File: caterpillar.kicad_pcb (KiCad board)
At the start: 2 copper layers, 20.2 x 20.2 mm, 32 parts, among them J1 Conn_ARM_JTAG_SWD_10, M1 Conn_01x02_Pin, M2 *, M3 Conn_01x02_Pin, U1 STBB1-APUR, U2 ASM330LHHTR, U3 DRV8212P, U4 ADP2503ACPZ-3.3-R7, U6 max5419leta+T

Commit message: rules: import design rules from Altium project ruleset
From altium_rules.RUL (36 rules, the importable subset):
- constraints: min track 4mil, min hole 4mil, hole-to-hole 9.75mil,
  copper-to-edge 10mil (was 0/disabled), min via dia 9mil
- solder mask expansion 4mil (was 0)
- new Power net class (12mil tracks) assigned to +3.3V/+BATT/VDC/GND
- caterpillar.kicad_dru: BLE_FEEDLINE scoped clearance (dormant until
  that class exists; its Altium width rule deliberately NOT imported -
  impedance-tuned to a different stackup) and 4mil courtyard clearance
- Default net class track width 0.2 -> 0.1524mm (6mil, user choice)
- remove stale radial dimension annotation on User.1
Altium autorouter rules (fanout/topology/priority) have no KiCad
equivalent; short-circuit/unrouted/antenna checks are built into DRC.
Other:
- rule pad_to_mask_clearance: 0 -> 0.1016
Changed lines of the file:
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@@
 			(dielectric_constraints no)
 		)
-		(pad_to_mask_clearance 0)
+		(pad_to_mask_clearance 0.1016)
 		(allow_soldermask_bridges_in_footprints no)
 		(tenting
@@
 		(capping no)
 		(filling no)
+		(zone_defaults)
 		(pcbplotparams
 			(layerselection 0x00000000_00000000_55555555_5555f550)
@@
 		)
 	)
-	(dimension
-		(type radial)
-		(layer "User.1")
-		(pts
-			(xy 118.2 100) (xy 128 99)
-		)
-		(leader_length 1.255801)
-		(format
-			(prefix "")
-			(suffix "")
-			(units 3)
-			(units_format 0)
-			(precision 6)
-			(suppress_zeroes yes)
-		)
-		(style
-			(thickness 0.1)
-			(arrow_length 0.5)
-			(text_position_mode 2)
-			(extension_offset 0.1)
-			(keep_text_aligned yes)
-		)
-		(gr_text "9.9"
-			(at 134.5 98.872519 0)
-			(layer "User.1")
-			(effects
-				(font
-					(size 1.5 1.5)
-					(thickness 0.3)
-				)
-			)
-		)
-	)

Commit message: reorganized design a lot for better space organization
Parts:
- removed 3.3V1, GND2, SCL1, SDA1: Conn_01x01_Pin, Connector_Wire:SolderWirePad_1x01_SMD_1x2mm
- removed M1: Conn_01x02_Pin, Connector_PinHeader_2.00mm:PinHeader_1x02_P2.00mm_Vertical
- removed M3: Conn_01x02_Pin, Connector_PinHeader_2.54mm:PinHeader_1x02_P2.54mm_Vertical
- added J2: SM02B-SRSS-TB_LF__SN_, SM02B-SRSS-TB:SM02BSRSSTBLFSN, F.Cu at (118.0, 107.8)
- added J3: Castellated_2PTH_P1.27mm, Castellated_2PTH_P1.27mm:Castellated_2PTH_P1.27mm, F.Cu at (111.3, 109.7)
- added J4: Castellated_2PTH_P1.27mm, Castellated_2PTH_P1.27mm:Castellated_2PTH_P1.27mm, F.Cu at (113.9, 109.7)
- C17, L1: moved to B.Cu
- moved U4 10.7 mm to (118.2, 107.7)
- moved L6 10.5 mm to (118.2, 104.5)
- moved C3 9.23 mm to (115.4, 105.5), turned to 90 degrees
- moved C11 8.83 mm to (113.8, 105.6), turned to 90 degrees
- moved U1 7.05 mm to (118.0, 97.7)
- moved C8 6.59 mm to (117.1, 102.2)
- moved L5 6.23 mm to (115.6, 92.4)
- moved U6 5.52 mm to (113.3, 98.5)
- moved L1 4.84 mm to (111.9, 91.8)
- moved C5 4.48 mm to (111.0, 102.3)
- moved C17 4.46 mm to (111.9, 94.7)
- moved C6 4.07 mm to (111.0, 105.5), turned to -90 degrees
- moved R4 3.87 mm to (112.4, 102.2), turned to 90 degrees
- moved C7 3.49 mm to (113.9, 102.2), turned to 90 degrees
- moved C1 3.19 mm to (117.2, 102.4)
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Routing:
- net GND: track 42.9 -> 6.13 mm, vias 10 -> 0
- net +3.3V: track 40.6 -> 5.80 mm, vias 6 -> 0
- net +BATT: track 20.6 -> 0.00 mm
- net /IMU_INT1: track 14.5 -> 0.00 mm, vias 2 -> 0
- net /SDA: track 10.3 -> 0.00 mm, vias 1 -> 0
- net /SCL: track 9.72 -> 0.00 mm, vias 1 -> 0
- net VDC: track 9.37 -> 0.00 mm, vias 1 -> 0
- net /IMU_INT2: track 8.47 -> 0.00 mm
- net /SHDN1: track 7.37 -> 0.00 mm, vias 1 -> 0
- net /OUT2: track 6.93 -> 0.00 mm
- net /OUT1: track 6.31 -> 0.00 mm
- net /FB: track 5.04 -> 0.00 mm
- net /IN2: track 1.61 -> 4.71 mm
- net /IN1: track 1.69 -> 4.24 mm
- net /M_SLP: track 1.77 -> 3.93 mm
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- added copper zone on In1.Cu, net GND
- removed copper zone on F.Cu, net +3.3V
- removed copper zone on F.Cu, net +BATT
- removed copper zone on B.Cu, net GND
- removed copper zone on F.Cu, net VDC
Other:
- board size 20.2 x 20.2 mm -> 18.3 x 20.3 mm
- copper layers 2 -> 4

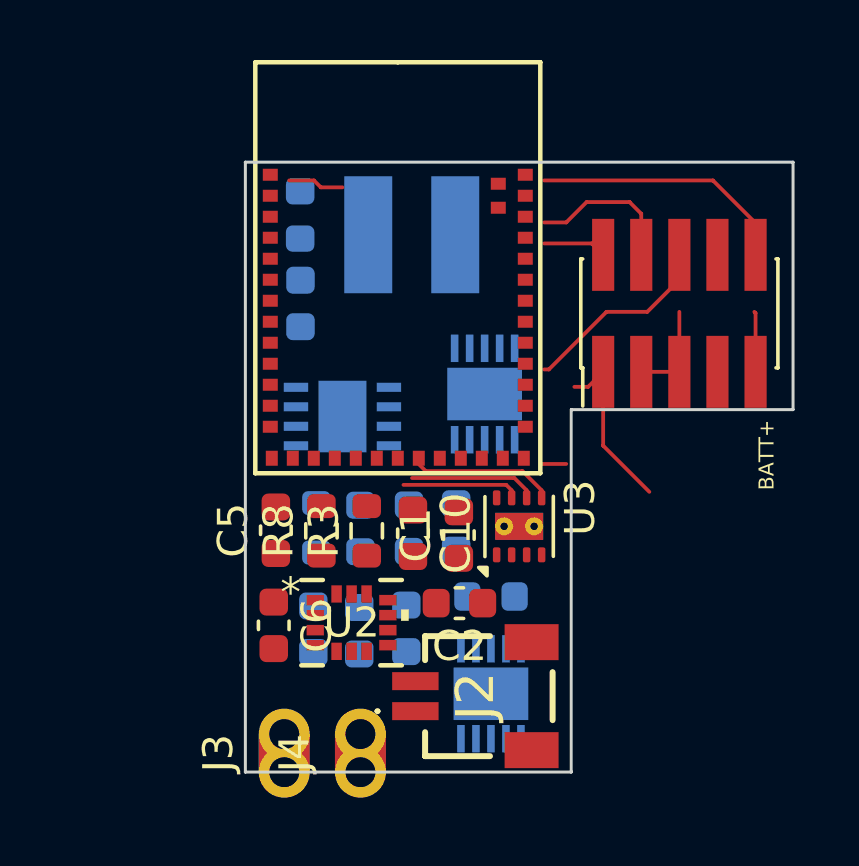
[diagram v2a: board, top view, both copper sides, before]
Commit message: component position&orientation adjusted further.
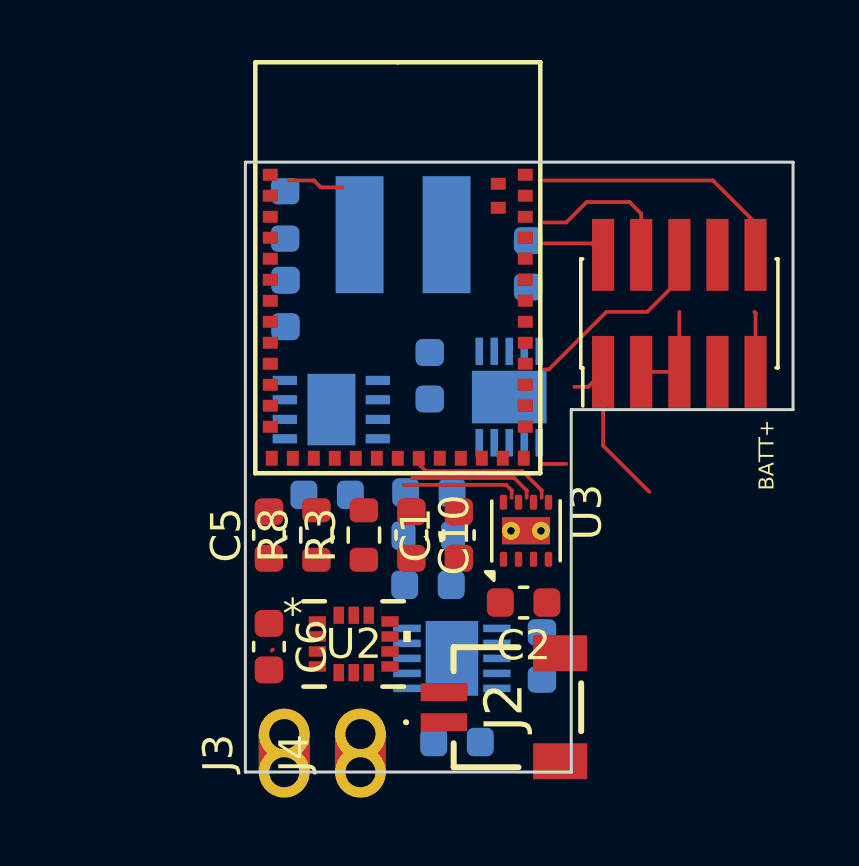
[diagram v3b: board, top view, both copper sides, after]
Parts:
- moved C11 13.5 mm to (119.5, 93.4)
- moved C9 5.13 mm to (116.2, 97.1), turned to -90 degrees
- moved C12 4.50 mm to (112.8, 101.1), turned to 180 degrees
- moved C3 4.15 mm to (117.1, 109.3), turned to 0 degrees
- moved R4 3.74 mm to (116.1, 102.5), turned to 0 degrees
- moved L6 2.61 mm to (119.9, 106.5), turned to 90 degrees
- moved C7 2.58 mm to (116.2, 101.0), turned to 0 degrees
- moved C8 2.15 mm to (116.1, 104.1), turned to 180 degrees
- moved C2 2.14 mm to (119.3, 104.7)
- moved U4 1.76 mm to (116.9, 106.5), turned to 180 degrees
- moved J2 1.02 mm to (118.9, 108.2)
- moved U1 0.83 mm to (118.8, 97.8)
- moved C6 0.73 mm to (110.8, 106.2)
- moved U2 0.71 mm to (113.6, 106.1)
- moved C17 0.50 mm to (111.4, 94.7)
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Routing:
- net /IN1: track 4.24 -> 0.00 mm
- net +3.3V: track 5.80 -> 9.74 mm

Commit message: pcb: sync with rev-2 schematic; bom: regenerate with MPN fields
- Board updated from schematic (re-linked by reference): C3/C6 uuid
  links repaired, orphan C7 footprint removed, R7/R9/C13/R5/R6 placed
  onto the board (placement/routing to follow)
- BOM regenerated from the current schematic (old caterpillar.csv was
  a stale Muscle_PCB-era export); grouped by value+footprint
- MPN stored as symbol fields in the schematic so BOM exports carry
  them automatically: C3/C11=GMC10X7R106K10NT (10uF 10V X7R 0603),
  C8/C9=CL10A226MP8NUNE (22uF 10V X5R 0603, DC-bias headroom for
  4.63V VDC), L6=LSCNB1608HKT1R5MD (1.5uH 1.3A 0603)
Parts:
- removed C7: 15pF, Capacitor_SMD:C_0603_1608Metric
- added C13: 100nF, Capacitor_SMD:C_0603_1608Metric, F.Cu at (105.6, 98.2)
- added R5: 100k, Resistor_SMD:R_0603_1608Metric, F.Cu at (105.6, 100.7)
- added R6: 100k, Resistor_SMD:R_0603_1608Metric, F.Cu at (105.6, 103.2)
- added R7: 100k, Resistor_SMD:R_0603_1608Metric, F.Cu at (105.6, 105.7)
- added R9: 12.1k, Resistor_SMD:R_0603_1608Metric, F.Cu at (105.6, 108.2)
- C6: value 10uF -> 100nF
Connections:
- M2 pad 2: unconnected-(M2-P1.09-Pad2) -> /CS
- M2 pad 3: unconnected-(M2-P1.10-Pad3) -> /SCLK
- M2 pad 4: unconnected-(M2-P1.11-Pad4) -> /VDC_SENSE
- M2 pad 6: unconnected-(M2-P1.13-Pad6) -> /MOSI
- M2 pad 7: unconnected-(M2-P1.14-Pad7) -> /MISO
- U1 pad 7: unconnected-(U1-MODE/SYNC-Pad7) -> GND
- U2 pad 1: GND -> /MISO
- U2 pad 12: +3.3V -> /CS
- U2 pad 13: /SCL -> /SCLK
- U2 pad 14: /SDA -> /MOSI
- U4 pad 7: unconnected-(U4-SYNC-Pad7) -> GND
- U6 pad 8: /FB -> /pot_H

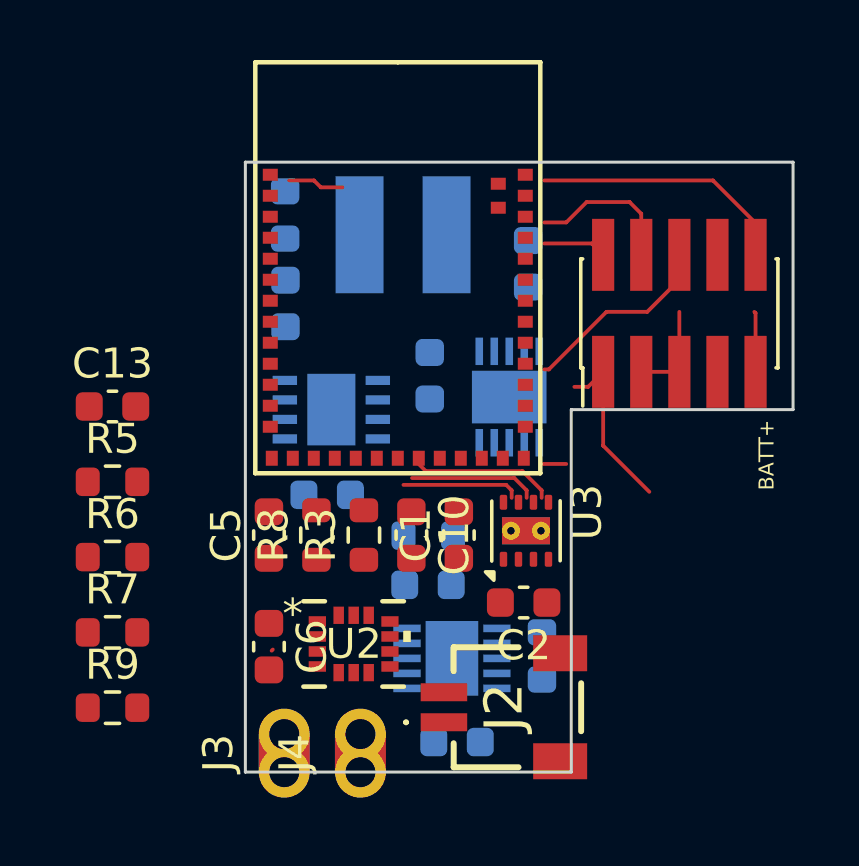
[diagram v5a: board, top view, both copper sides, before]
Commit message: zones created, power layer set up well that VDC, 3V3, and BATT grouped together by planes, GND layer added. Decoupling Caps position checked
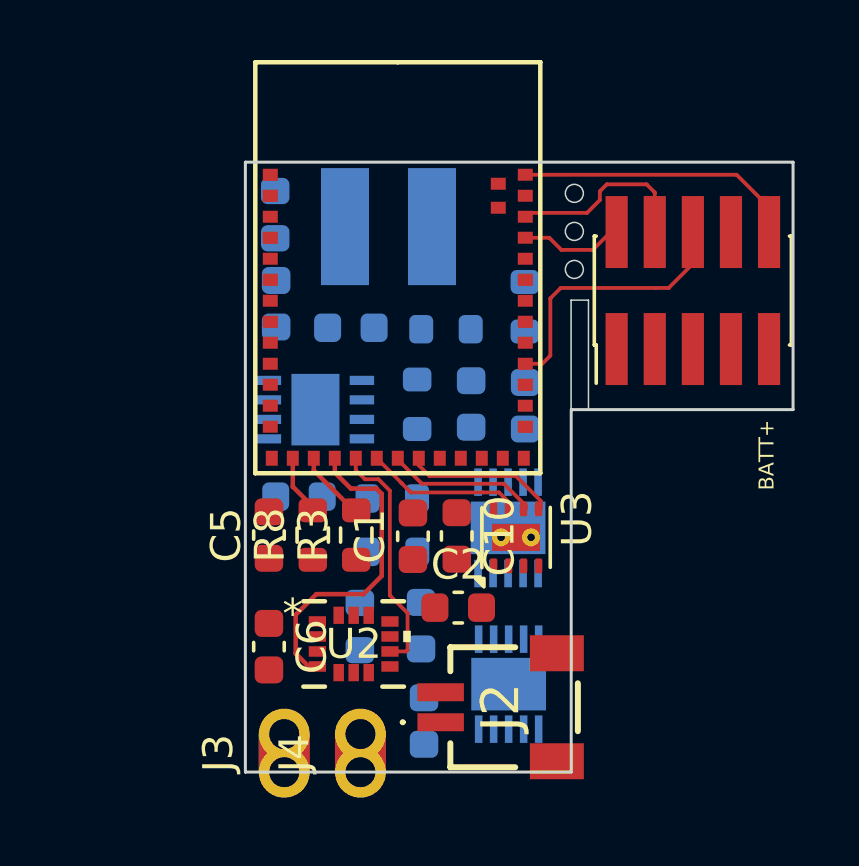
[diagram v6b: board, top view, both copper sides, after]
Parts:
- C13, R5, R6, R7, R9: moved to B.Cu
- moved R7 17.5 mm to (119.3, 94.8), turned to -90 degrees
- moved R5 12.2 mm to (116.7, 95.6), turned to 180 degrees
- moved R9 11.6 mm to (114.9, 101.2)
- moved R6 11.4 mm to (115.8, 98.1), turned to -90 degrees
- moved C13 8.37 mm to (113.5, 95.5)
- moved L6 6.15 mm to (113.8, 105.5), turned to -90 degrees
- moved C11 4.73 mm to (119.4, 98.1)
- moved U1 4.36 mm to (118.8, 102.2)
- moved C2 2.19 mm to (117.1, 104.9), turned to 0 degrees
- moved U4 2.08 mm to (118.8, 107.4), turned to -90 degrees
- moved C9 1.67 mm to (117.6, 98.1)
- moved C1 1.53 mm to (115.6, 102.5)
- moved C10 1.51 mm to (117.1, 102.5)
- moved C8 1.38 mm to (115.9, 105.5), turned to -90 degrees
- moved R4 1.31 mm to (114.9, 103.0), turned to 180 degrees
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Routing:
- net /IMU_INT1: track 0.00 -> 10.7 mm
- net +3.3V: track 9.74 -> 0.00 mm
- net /IMU_INT2: track 0.00 -> 7.98 mm
- net GND: track 6.13 -> 0.00 mm
- net /IN1: track 0.00 -> 5.10 mm
- net /SWO: track 6.57 -> 9.97 mm
- net /SCL: track 0.00 -> 2.63 mm
- net /SDA: track 0.00 -> 2.06 mm
- net Net-(U1-SW2): track 1.87 -> 0.00 mm
- net /SWDIO: track 2.12 -> 3.54 mm
- net /SWDCLK: track 5.05 -> 6.17 mm
- net /M_SLP: track 4.24 -> 5.26 mm
- net /nRST: track 8.69 -> 9.20 mm
- added copper zone on In1.Cu, net +3.3V
- added copper zone on In1.Cu, net +BATT
- added copper zone on In2.Cu, net GND
- added copper zone on In1.Cu, net VDC
- removed copper zone on In1.Cu, net GND
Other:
- outline, holes or cut-outs redrawn

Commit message: all nets conencted
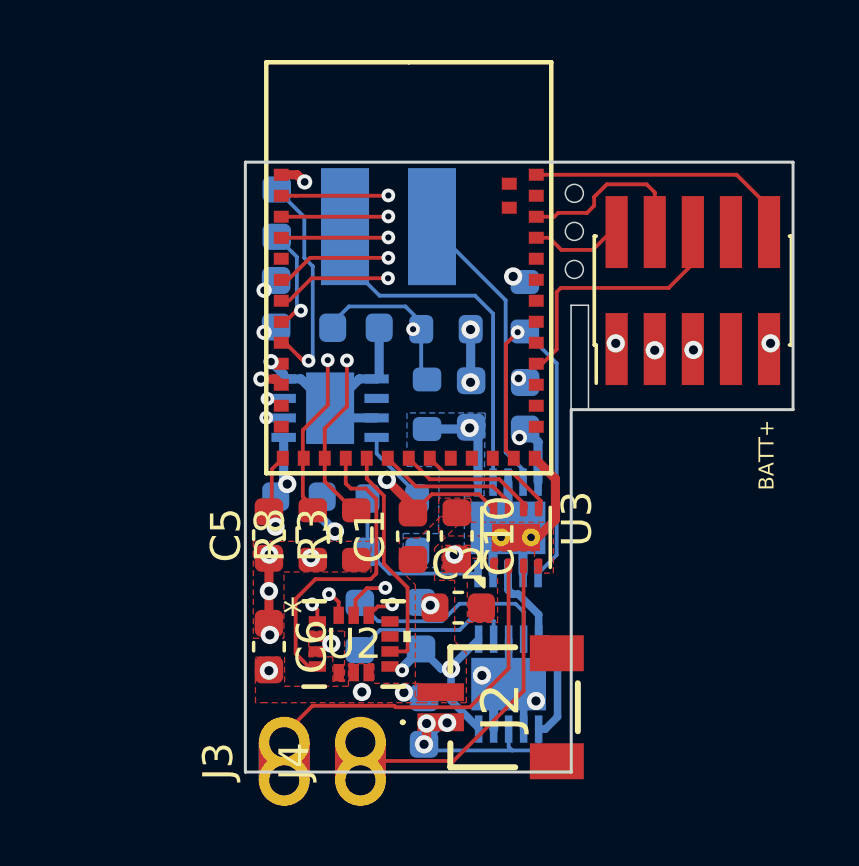
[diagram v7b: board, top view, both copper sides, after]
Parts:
- moved G*** 10.3 mm to (111.8, 103.7)
- moved U6 0.49 mm to (112.9, 98.2)
- moved M2 0.37 mm to (115.5, 86.7)
- moved R6 0.33 mm to (116.1, 98.1)
- moved J3 0.27 mm to (111.3, 110.0)
- moved J4 0.27 mm to (113.9, 110.0)
- moved C13 0.17 mm to (113.7, 95.5)
- moved L1 0.07 mm to (111.1, 91.7), turned to -90 degrees
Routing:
- net GND: track 0.00 -> 26.8 mm, vias 0 -> 18
- net /CS: track 0.00 -> 19.3 mm, vias 0 -> 2
- net /SCLK: track 0.00 -> 18.7 mm, vias 0 -> 2
- net /MOSI: track 0.00 -> 16.9 mm, vias 0 -> 2
- net /MISO: track 0.00 -> 16.2 mm, vias 0 -> 2
- net +BATT: track 0.00 -> 15.6 mm, vias 0 -> 4
- net +3.3V: track 0.00 -> 15.2 mm, vias 0 -> 12
- net /SHDN1: track 0.00 -> 13.2 mm, vias 0 -> 1
- net /VDC_SENSE: track 0.00 -> 12.6 mm, vias 0 -> 2
- net Net-(U1-SW2): track 0.00 -> 12.4 mm
- net /OUT1: track 0.00 -> 11.8 mm
- net /OUT2: track 0.00 -> 10.7 mm
- net Net-(U1-SW1): track 0.00 -> 9.77 mm
- net Net-(M2-DCC): track 0.00 -> 7.63 mm, vias 0 -> 1
- net Net-(U4-SW1): track 0.00 -> 6.98 mm
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- added copper zone on F.Cu, net +3.3V
- added copper zone on F.Cu, net GND
- added copper zone on B.Cu, net VDC
- added copper zone on F.Cu, net VDC
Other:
- outline, holes or cut-outs redrawn
